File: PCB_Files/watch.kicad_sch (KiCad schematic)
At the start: 118 parts, among them J1 Conn_01x13_MountingPin, J3 Conn_01x02_Pin, P1 USB_C_Plug_USB2.0, Q1 BC847, Q2 BC847, Q3 FS8205A, Q4 BSS138, Q5 BSS138, Q8 BC847, SW1 SW_Push, SW2 SW_Push, U1 APS6404L-3SQRx-ZR, U10 LSM6DS3, U11 MAX-M10S, U12 MCP1700x-120xxMB, U13 DRV2605LDGS, U2 ESP32-PICO-D4, U3 CP2102N-Axx-xQFN28, U4 TPS7A0533PDBV, U5 MCP73831-2-OT, U6 AP9101CK6, U7 MAX30105EFD_T, U8 W25Q128JVS, U9 BMP388, Y1 SG-3030CM

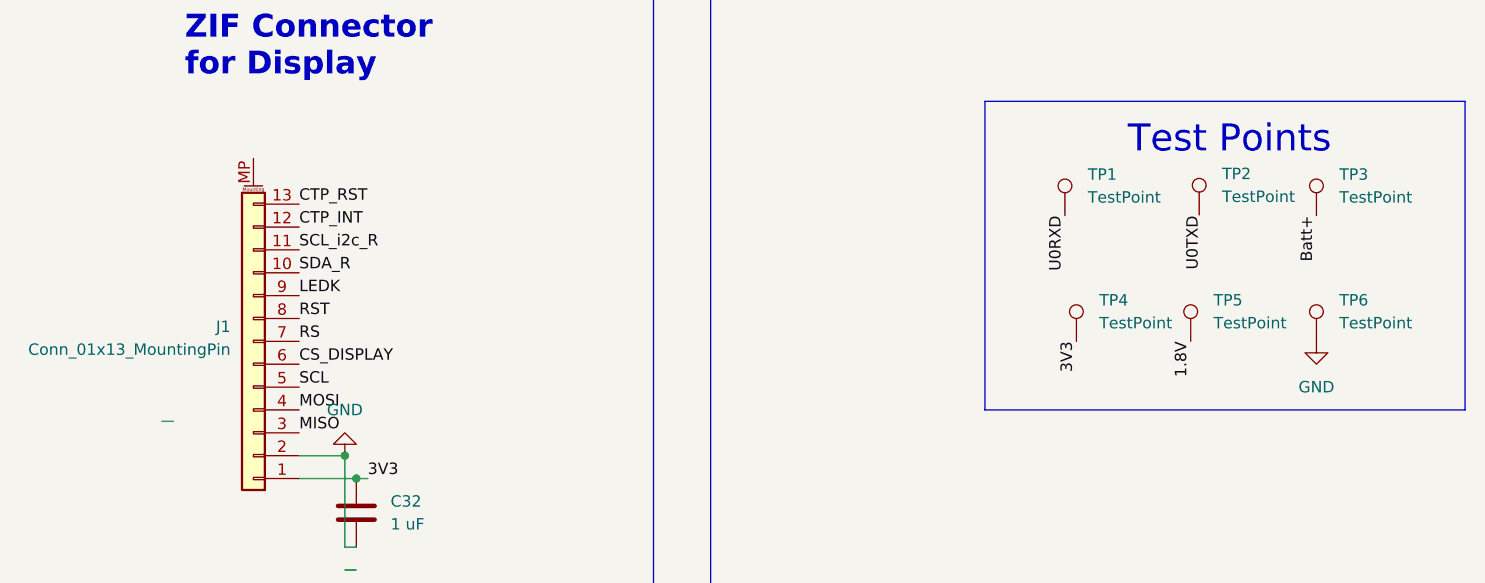
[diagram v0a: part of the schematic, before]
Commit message: Added new ZIF connector footprint and made changes in schematics
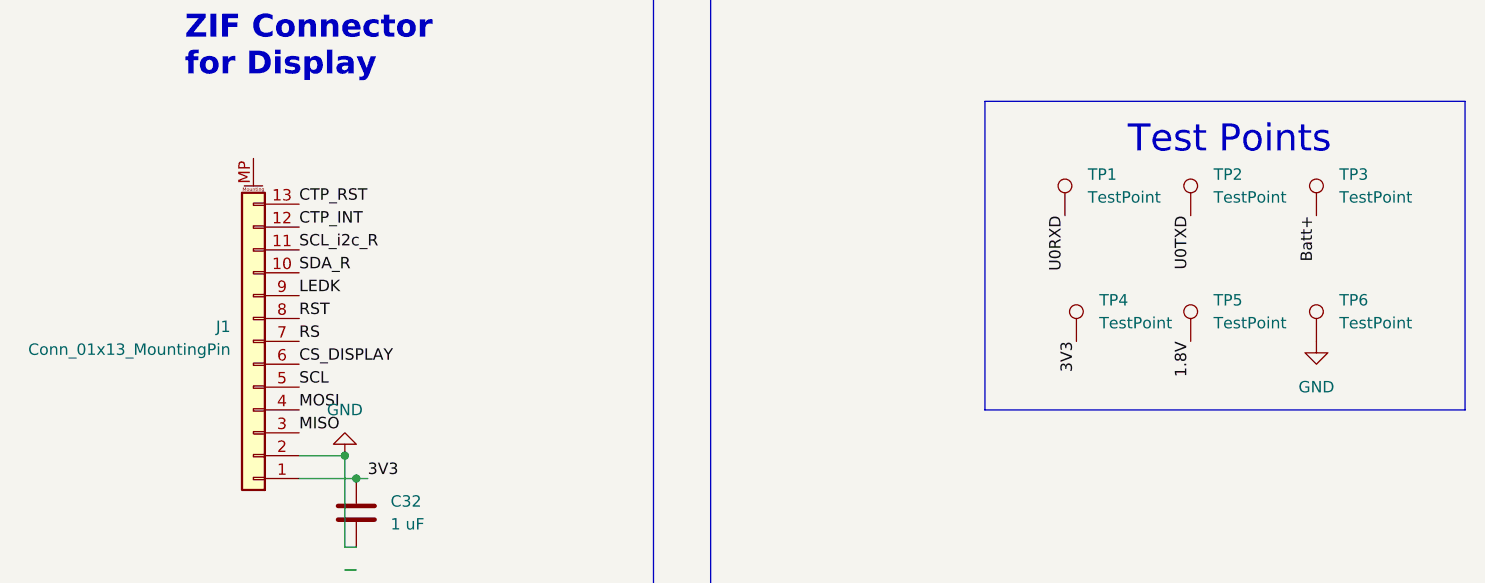
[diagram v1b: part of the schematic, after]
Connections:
- net U0TXD: now also TP2.1
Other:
- moved on the sheet: TP2
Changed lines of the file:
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@@
 	(wire
 		(pts
-			(xy 408.94 307.34) (xy 410.21 307.34)
-		)
-		(stroke
-			(width 0)
-			(type default)
-		)
-	)
-	(wire
-		(pts
 			(xy 302.26 72.39) (xy 311.15 72.39)
 		)
@@
 	)
 	(label "U0TXD"
-		(at 524.51 284.48 270)
+		(at 523.24 284.48 270)
 		(effects
 			(font
@@
 	(symbol
 		(lib_id "Connector:TestPoint")
-		(at 524.1854 284.4073 0)
+		(at 523.24 284.48 0)
 		(unit 1)
 		(exclude_from_sim no)
@@
 		(fields_autoplaced yes)
 		(property "Reference" "TP2"
-			(at 526.7254 279.8352 0)
+			(at 525.78 279.9079 0)
 			(effects
 				(font
@@
 		)
 		(property "Value" "TestPoint"
-			(at 526.7254 282.3752 0)
+			(at 525.78 282.4479 0)
 			(effects
 				(font
@@
 		)
 		(property "Footprint" "TestPoint:TestPoint_Pad_D1.0mm"
-			(at 529.2654 284.4073 0)
+			(at 528.32 284.48 0)
 			(effects
 				(font
@@
 		)
 		(property "Datasheet" "~"
-			(at 529.2654 284.4073 0)
+			(at 528.32 284.48 0)
 			(effects
 				(font
@@
 		)
 		(property "Description" "test point"
-			(at 524.1854 284.4073 0)
+			(at 523.24 284.48 0)
 			(effects
 				(font

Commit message: Adding missing footprints and making cAD
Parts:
- removed J1: Conn_01x13_MountingPin, footprints:HRS_FH34SRJ-12S-0.5SH_50_, symbol Connector_Generic_MountingPin:Conn_01x13_MountingPin
- removed R8: 330, Resistor_SMD:R_0603_1608Metric, symbol Device:R
- added J2: Conn_01x14_MountingPin, footprints:HRS_FH34SRJ-14S-0.5SH_50_, symbol Connector_Generic_MountingPin:Conn_01x14_MountingPin
- added TP7, TP8: TestPoint, TestPoint:TestPoint_Pad_D1.0mm, symbol Connector:TestPoint
- D1: footprint Diode_SMD:D_SMA -> Capacitor_SMD:C_0603_1608Metric
- P1: footprint Connector_USB:USB_C_Receptacle_GCT_USB4125-xx-x-0190_6P_TopMnt_Horizontal -> Connector_USB:USB_C_Receptacle_GCT_USB4105-xx-A_16P_TopMnt_Horizontal
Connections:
- net 3V3: now also J2.1 (Pin_1)
- net BTN1: now also TP7.1
- net BTN2: now also TP8.1
- net CS_DISPLAY: now also J2.6 (Pin_6)
- net CTP_INT: now also J2.12 (Pin_12)
- net CTP_RST: now also J2.13 (Pin_13)
- net GND: now also D4.1 (K), U8.4 (GND), J2.2 (Pin_2)
- net LEDK: now also J2.9 (Pin_9)
- net MISO: now also J2.3 (Pin_3)
- net MOSI: now also J2.4 (Pin_4)
- net RS: now also J2.7 (Pin_7)
- net RST: now also J2.8 (Pin_8)
- net SCL: now also J2.5 (Pin_5)
- net SCL_i2c: now also J2.11 (Pin_11)
- net SDA: now also J2.10 (Pin_10)
- no-connect marks 34 -> 35
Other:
- moved on the sheet: C32

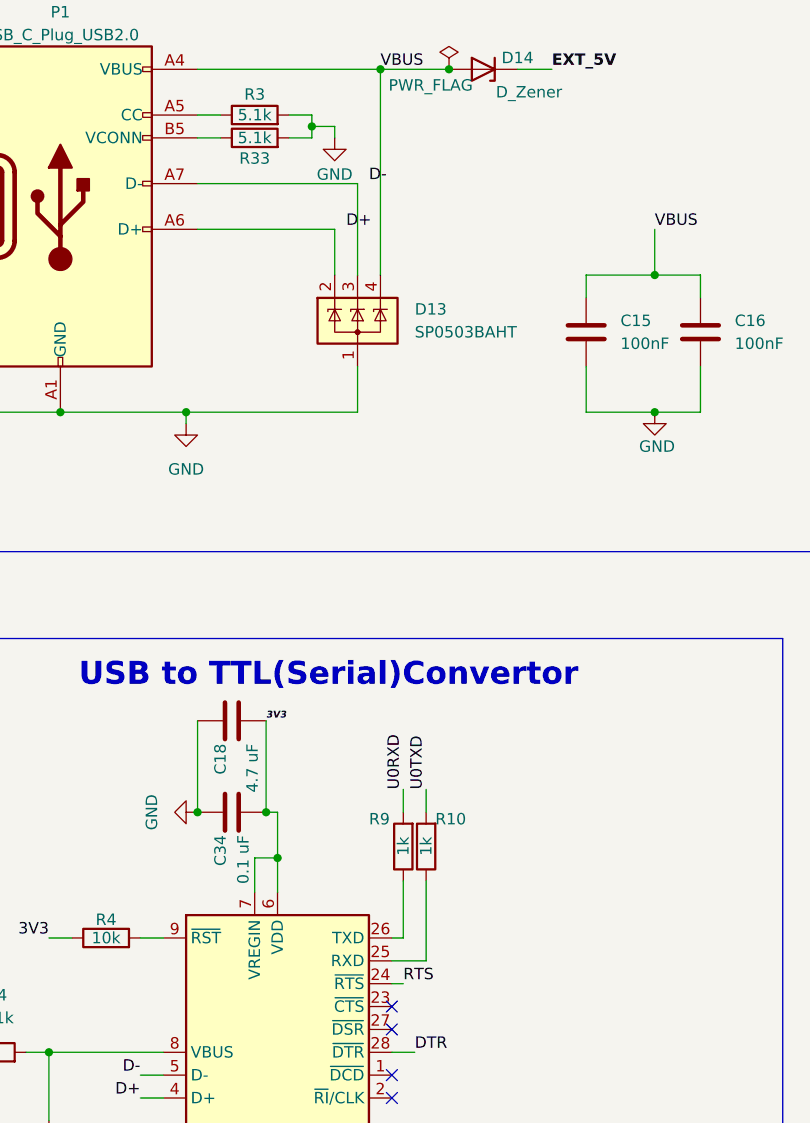
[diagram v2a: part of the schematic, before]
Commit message: changed place of some components and fixed antenna
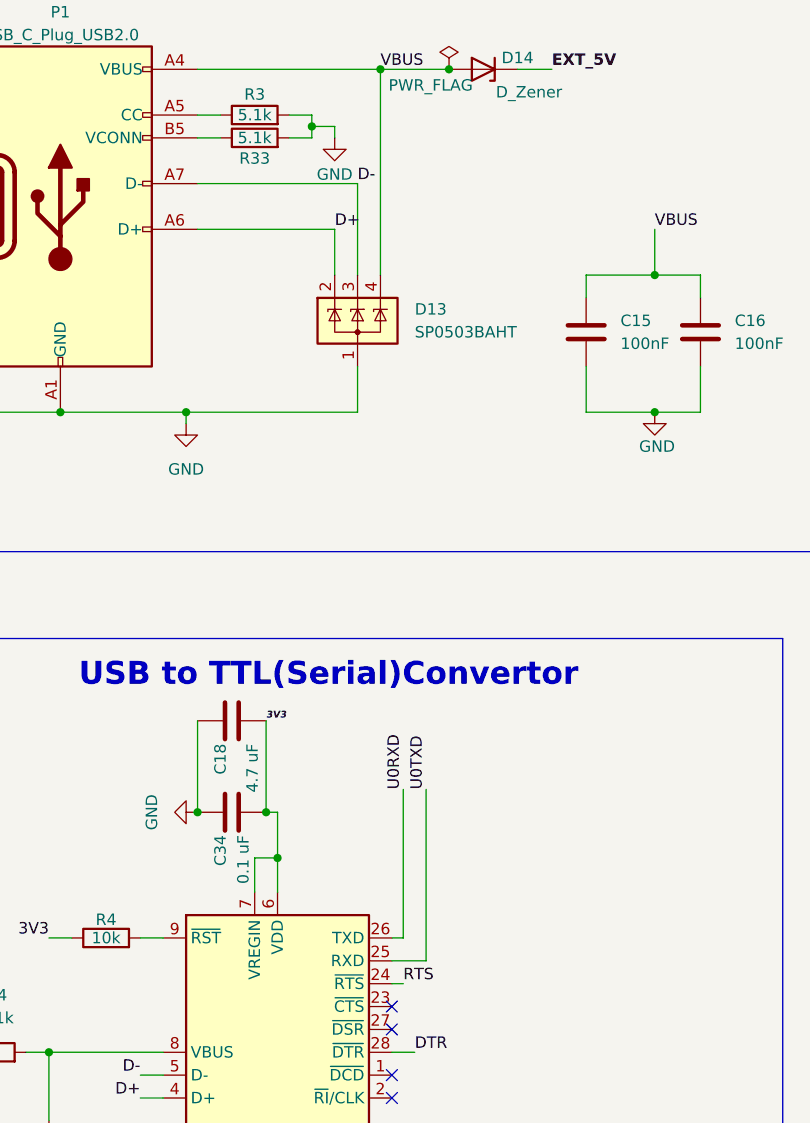
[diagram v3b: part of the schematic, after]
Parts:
- removed R10, R9: 1k, Resistor_SMD:R_0603_1608Metric, symbol Device:R
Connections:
- net D+: now also D13.2 (K), P1.A6 (D+)
- net D-: now also D13.3 (K), P1.A7 (D-)
- net U0RXD: now also U3.26 (TXD)
- net U0TXD: now also U3.25 (RXD)
- net at D6.2 (A2), FB1.1, U11.11 (RF_IN): now also AE1.3 (A); no longer AE1.1 (A)
- net at C36.1, L2.2: now also AE2.3 (A); no longer AE2.1 (A)
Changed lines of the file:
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@@
 	(wire
 		(pts
-			(xy 237.49 152.4) (xy 237.49 161.29)
-		)
-		(stroke
-			(width 0)
-			(type default)
-		)
-	)
-	(wire
-		(pts
 			(xy 363.22 96.52) (xy 368.3 96.52)
 		)
@@
 	(wire
 		(pts
-			(xy 237.49 142.24) (xy 237.49 144.78)
+			(xy 237.49 142.24) (xy 237.49 161.29)
 		)
 		(stroke
@@
 	(wire
 		(pts
-			(xy 234.95 152.4) (xy 234.95 158.75)
+			(xy 234.95 142.24) (xy 234.95 158.75)
 		)
 		(stroke
@@
 	(wire
 		(pts
-			(xy 234.95 142.24) (xy 234.95 144.78)
-		)
-		(stroke
-			(width 0)
-			(type default)
-		)
-	)
-	(wire
-		(pts
 			(xy 102.87 72.39) (xy 116.84 72.39)
 		)
@@
 	)
 	(label "D+"
-		(at 228.6 80.01 0)
+		(at 227.33 80.01 0)
 		(effects
 			(font
@@
 	)
 	(label "D-"
-		(at 231.14 74.93 0)
+		(at 229.87 74.93 0)
 		(effects
 			(font
@@
 	)
 	(symbol
+		(lib_name "Antenna_Shield_1")
 		(lib_id "Device:Antenna_Shield")
 		(at 115.57 212.09 0)
@@
 			)
 		)
-		(pin "1"
+		(pin "3"
 		)
 		(pin "2"
@@
 	)
 	(symbol
-		(lib_id "Device:R")
-		(at 234.95 148.59 180)
-		(unit 1)
-		(exclude_from_sim no)
-		(in_bom yes)
-		(on_board yes)
-		(dnp no)
-		(property "Reference" "R9"
-			(at 231.14 145.542 0)
-			(effects
-				(font
-					(size 1.27 1.27)
-				)
-				(justify right)
-			)
-		)
-		(property "Value" "1k"
-			(at 234.95 149.606 90)
-			(effects
-				(font
-					(size 1.27 1.27)
-				)
-				(justify right)
-			)
-		)
-		(property "Footprint" "Resistor_SMD:R_0603_1608Metric"
-			(at 236.728 148.59 90)
-			(effects
-				(font
-					(size 1.27 1.27)
-				)
-				(hide yes)
-			)
-		)
-		(property "Datasheet" "~"
-			(at 234.95 148.59 0)
-			(effects
-				(font
-					(size 1.27 1.27)
-				)
-				(hide yes)
-			)
-		)
-		(property "Description" "Resistor"
-			(at 234.95 148.59 0)
-			(effects
-				(font
-					(size 1.27 1.27)
-				)
-				(hide yes)
-			)
-		)
-		(pin "2"
-		)
-		(pin "1"
-		)
-		(instances
-			(project "watch"
-				(path "/0f9276a0-1239-442e-9bc6-369ba5509075"
-					(reference "R9")
-					(unit 1)
-				)
-			)
-		)
-	)
-	(symbol
 		(lib_id "Device:LED")
 		(at 438.15 177.8 90)
@@
 			)
 		)
-		(pin "1"
+		(pin "3"
 		)
 		(pin "2"
@@
 					(unit 1)
 				)
-			)
-		)
-	)
-	(symbol
-		(lib_id "Device:R")
-		(at 237.49 148.59 180)
-		(unit 1)
-		(exclude_from_sim no)
-		(in_bom yes)
-		(on_board yes)
-		(dnp no)
-		(property "Reference" "R10"
-			(at 238.506 145.542 0)
-			(effects
-				(font
-					(size 1.27 1.27)
-				)
-				(justify right)
-			)
-		)
-		(property "Value" "1k"
-			(at 237.49 149.606 90)
-			(effects
-				(font
-					(size 1.27 1.27)
-				)
-				(justify right)
-			)
-		)
-		(property "Footprint" "Resistor_SMD:R_0603_1608Metric"
-			(at 239.268 148.59 90)
-			(effects
-				(font
-					(size 1.27 1.27)
-				)
-				(hide yes)
-			)
-		)
-		(property "Datasheet" "~"
-			(at 237.49 148.59 0)
-			(effects
-				(font
-					(size 1.27 1.27)
-				)
-				(hide yes)
-			)
-		)
-		(property "Description" "Resistor"
-			(at 237.49 148.59 0)
-			(effects
-				(font
-					(size 1.27 1.27)
-				)
-				(hide yes)
-			)
-		)
-		(pin "2"
-		)
-		(pin "1"
-		)
-		(instances
-			(project "watch"
-				(path "/0f9276a0-1239-442e-9bc6-369ba5509075"
-					(reference "R10")
-					(unit 1)
-				)

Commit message: Making major changes in the schematic, added a external 40MHz crystal oscilator and did routing
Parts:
- removed C20: 10 uF, Capacitor_SMD:C_0603_1608Metric, symbol Device:C
- removed D14: D_Zener, Diode_SMD:D_0603_1608Metric, symbol Device:D_Zener
- removed D3, D5: LED, LED_SMD:LED_0603_1608Metric, symbol Device:LED
- removed Q3: FS8205A, footprints:SOP65P640X120-8N, symbol FS8205A:FS8205A
- removed R13: 2.7k, Resistor_SMD:R_0603_1608Metric, symbol Device:R
- removed R14, R15: 330, Resistor_SMD:R_0603_1608Metric, symbol Device:R
- removed R16: 2k, Resistor_SMD:R_0603_1608Metric, symbol Device:R
- removed R17, R30: 0R, Resistor_SMD:R_0603_1608Metric, symbol Device:R
- removed U4: TPS7A0533PDBV, Package_TO_SOT_SMD:SOT-23-5, symbol Regulator_Linear:TPS7A0533PDBV
- removed U5: MCP73831-2-OT, Package_TO_SOT_SMD:SOT-23-5, symbol Battery_Management:MCP73831-2-OT
- removed U6: AP9101CK6, Package_TO_SOT_SMD:SOT-23-6, symbol Battery_Management:AP9101CK6
- removed Y1: SG-3030CM, Oscillator:Oscillator_SMD_SeikoEpson_SG3030CM, symbol Oscillator:SG-3030CM
- added C23: 1uF, Capacitor_SMD:C_0603_1608Metric, symbol Device:C
- added C33: 4.7uF, Capacitor_SMD:C_0603_1608Metric, symbol Device:C
- added D2, D7, D8: LED, LED_SMD:LED_0603_1608Metric, symbol Device:LED
- added D9: SS14FL, footprints:SOD-123FL, symbol Diode:SS14
- added J1: Conn_01x02_Pin, Connector_PinHeader_1.00mm:PinHeader_1x02_P1.00mm_Vertical, symbol Connector:Conn_01x02_Pin
- added R10: 1.18k, Resistor_SMD:R_0603_1608Metric, symbol Device:R
- added R24: 1.13k, Resistor_SMD:R_0603_1608Metric, symbol Device:R
- added R25, R42: 1.5k, Resistor_SMD:R_0603_1608Metric, symbol Device:R
- added R43: 10k, Resistor_SMD:R_0603_1608Metric, symbol Device:R
- added R6: 0.3k, Resistor_SMD:R_0603_1608Metric, symbol Device:R
- added R8: 0R, Resistor_SMD:R_0603_1608Metric, symbol Device:R
- added R9: 4.12k, Resistor_SMD:R_0603_1608Metric, symbol Device:R
- added U14: TLV75533PDBV, Package_TO_SOT_SMD:SOT-23-5, symbol Regulator_Linear:TLV75533PDBV
- added U15: BQ24074RGT, Package_DFN_QFN:VQFN-16-1EP_3x3mm_P0.5mm_EP1.6x1.6mm, symbol Battery_Management:BQ24074RGT
- added XTAL1: ECS-400-10-37B2-CKY-TR, footprints:ECX-1637B2_ECS, symbol symbol:ECS-400-10-37B2-CKY-TR
- added XTAL2: FC-135R 32.7680KA-A3, footprints:XTAL_KA-A3_EPS, symbol crystal_oss_32K:FC-135R_32.7680KA-A3
- C15, C16: value 100nF -> 22uF
- C17: value 1 uF -> 0.1 uF
- C4: value 0.1 uF -> 12.5pF
- C5: value 0.1 uF -> 8pF
- C6: value 4.7 uF -> 10pF
- C7: value 4.7 uF -> 12.5pF
- R7: value 330 -> 10k
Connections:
- net C5 is gone; now on an unnamed net: C5.1
- net 3V3: now also C16.1, C17.2, C19.2, R6.1, U14.5 (OUT); no longer C19.1, C4.1
- net Batt+: now also C15.1, C33.1, R25.1, R42.1, U14.1 (IN), U14.3 (EN), U15.10 (OUT), U15.11 (OUT), U15.5 (EN2); no longer C17.1, C7.1
- net EN: now also J2.13 (Pin_13), J2.8 (Pin_8)
- net GND: now also C17.1, C19.1, C6.1, C23.2, C33.2, D8.1 (K), J1.2 (Pin_2), R10.2, R24.2, R43.2, R9.2, U14.2 (GND), U15.14 (TMR), U15.17 (VSS), U15.4 (~{CE}), U15.6 (EN1), U15.8 (VSS), XTAL1.2 (GND), XTAL1.4 (GND); no longer C17.2, C19.2, C6.2, R7.2
- net RS: now also U2.17 (IO14); no longer U2.13 (IO33)
- net VBUS: now also D9.2 (A); no longer C15.1, C16.1, C6.1, R34.1
- net XTAL_N: now reaches U2.44 (XTAL_N)
- net XTAL_N: now also C6.2, XTAL1.3 (OUT/IN)
- net XTAL_P: now reaches U2.45 (XTAL_P)
- net XTAL_P: now also R7.2
- net at R7.1: now also XTAL1.1 (IN/OUT)
- net 32K_XP renamed 32K_P
- net 32K_P: now also C4.1, R8.1, XTAL2.1
- removed net CTP_RST: J2.13 (Pin_13), U2.17 (IO14)
- net RST: no longer names the net of U2.15 (IO26)
- net RST: no longer J2.8 (Pin_8)
- new net: R9.1, U15.15 (ITERM)
- new net: R24.1, U15.16 (ISET)
- new net: D8.2 (A), R6.2
- new net: D2.1 (K), U15.7 (~{PGOOD})
- new net: D2.2 (A), R42.2
- new net: D7.2 (A), R25.2
- new net: R43.1, U15.1 (TS)
- new net: D7.1 (K), U15.9 (~{CHG})
- new net: R10.1, U15.12 (ILIM)
- new net 32K_N: C7.1, R8.2, U2.13 (IO33), XTAL2.2
- new net BAT+: J1.1 (Pin_1), U15.2 (BAT), U15.3 (BAT)
- new net EXT_5V: C23.1, D9.1 (K), R34.1, U15.13 (IN)
- no-connect marks 35 -> 36
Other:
- note added: "Battery"
- note added: "External 40MHz"
- note added: "Second osscilator"
- note removed: "Battery Protection Module"
- note removed: "Charging Module"
- note removed: "Crystal Oscillator"
- moved on the sheet: C37, U1

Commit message: Made changes in schematic and routing
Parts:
- removed C5: 8pF, Capacitor_SMD:C_0603_1608Metric, symbol Device:C
- removed C6: 10pF, Capacitor_SMD:C_0603_1608Metric, symbol Device:C
- removed R7: 10k, Resistor_SMD:R_0603_1608Metric, symbol Device:R
- removed U8: W25Q128JVS, footprints:SOIC-8_5.23x5.23mm_P1.27mm, symbol Memory_Flash:W25Q128JVS
- removed XTAL1: ECS-400-10-37B2-CKY-TR, footprints:ECX-1637B2_ECS, symbol symbol:ECS-400-10-37B2-CKY-TR
- added U4: W25Q128JVP, Package_SON:WSON-8-1EP_6x5mm_P1.27mm_EP3.4x4.3mm, symbol Memory_Flash:W25Q128JVP
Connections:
- net 3V3: now also U4.8 (VCC)
- net BL_PWM: no longer R37.1
- net CE: now also U2.29 (SD3/IO10); no longer U2.24 (IO4)
- net CS_ROM: now also U4.1 (~{CS})
- net GND: now also U4.4 (GND); no longer Q8.2 (E)
- net LEDK: no longer R36.2
- net MISO: now also U2.15 (IO26); no longer U2.28 (SD2/IO9)
- net MOSI: now also U2.24 (IO4); no longer U2.29 (SD3/IO10)
- net VSPICLK: now also U4.6 (CLK); no longer U1.6 (SCLK)
- net VSPID: now also U4.5 (DI/IO_{0}); no longer U1.5 (SI/SIO0)
- net VSPIHD: now also U4.7 (~{HOLD}/~{RESET}/IO_{3}); no longer U1.7 (SIO3)
- net VSPIQ: now also U4.2 (DO/IO_{1}); no longer U1.2 (SO/SIO1)
- net VSPIWP: now also U4.3 (~{WP}/IO_{2}); no longer U1.3 (SIO2)
- net VSPIHD_RAM: now reaches U2.30 (CMD)
- net VSPIHD_RAM: now also U1.7 (SIO3)
- net VSPICLK_RAM: now reaches U2.31 (CLK)
- net VSPICLK_RAM: now also U1.6 (SCLK)
- net VSPIQ_RAM: now reaches U2.32 (SD0)
- net VSPIQ_RAM: now also U1.2 (SO/SIO1)
- net VSPID_RAM: now reaches U2.33 (SD1)
- net VSPID_RAM: now also U1.5 (SI/SIO0)
- removed net XTAL_N: U2.44 (XTAL_N)
- removed net XTAL_P: U2.45 (XTAL_P)
- new net VSPIWP_RAM: U1.3 (SIO2), U2.28 (SD2/IO9)
- no-connect marks 36 -> 34
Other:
- note removed: "External 40MHz"
- moved on the sheet: C37, C39, Q8, R36, R37, U1
